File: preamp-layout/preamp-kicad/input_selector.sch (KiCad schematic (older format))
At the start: 40 parts, among them J54 Conn_01x03_Female, J55 Conn_01x03_Male, J56 Conn_01x03_Male, J57 Conn_01x03_Male, J58 Conn_01x03_Male, J59 Conn_01x07_Female, J60 Conn_01x07_Female, J61 Conn_01x03_Male, J62 Conn_01x03_Male, J63 Conn_01x03_Female, J64 Conn_01x02_Female, J65 Conn_01x02_Male, J66 Conn_01x03_Female, J67 Conn_01x03_Female, K1 G6JU, K2 G6JU, K3 G6JU, K4 G6JU, K5 G6JU, K6 G6JU, K7 G6JU, U17 MCP23S17_SP, U18 ULN2003, U19 ULN2003

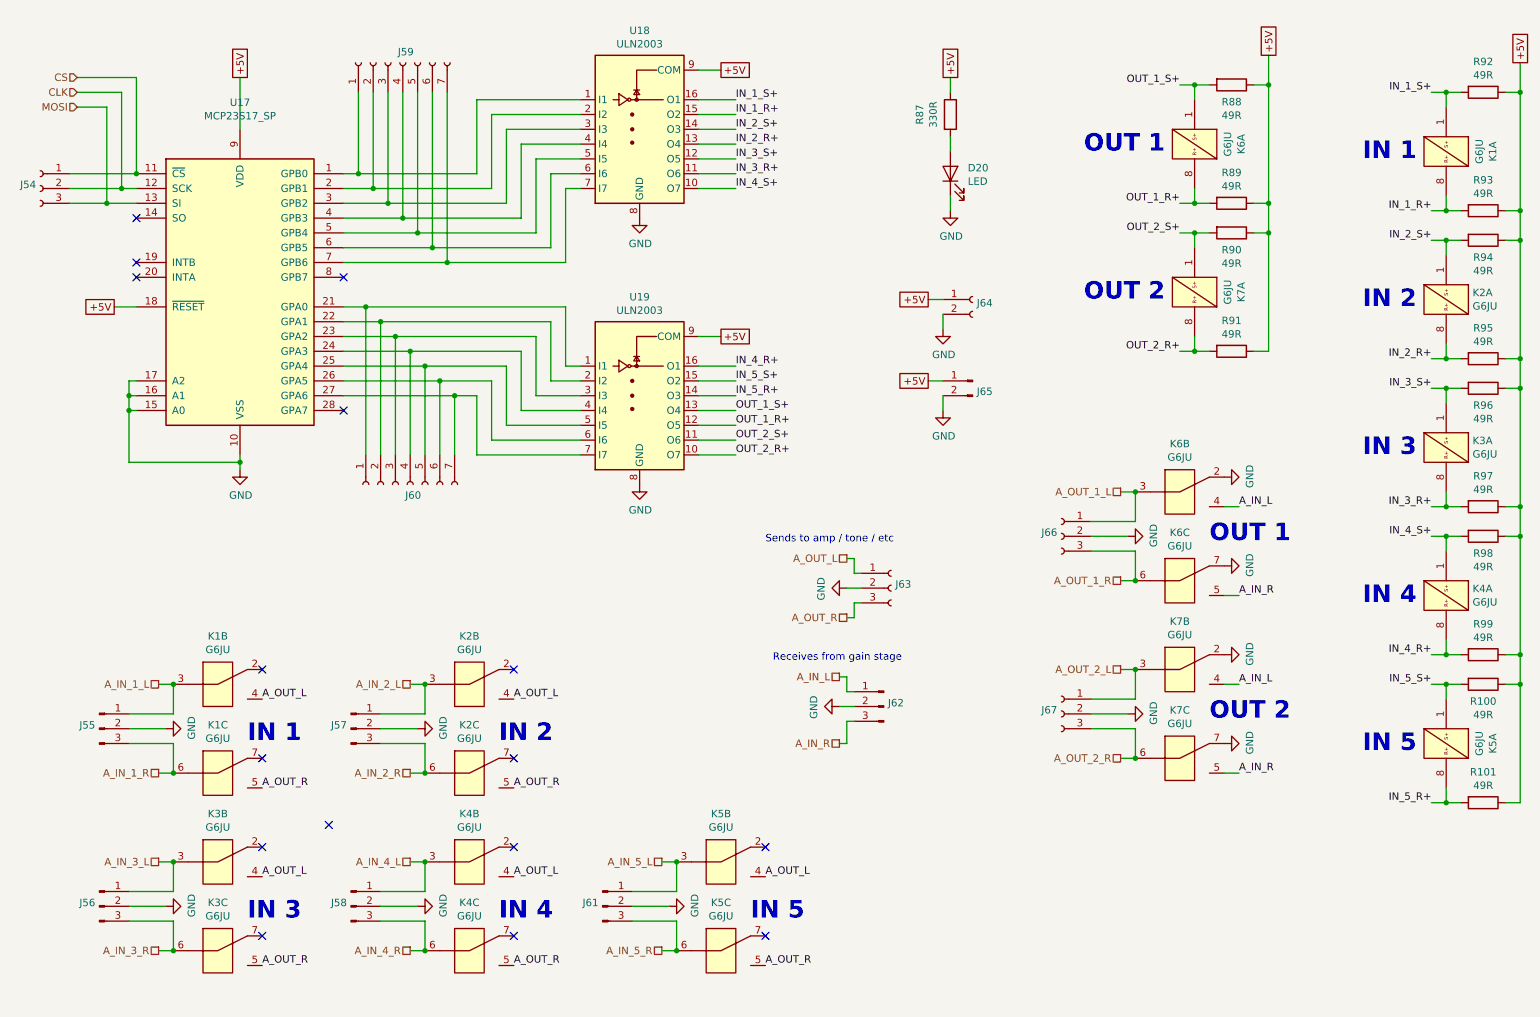
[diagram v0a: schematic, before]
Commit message: AC PCB Update
Removed Switch symbol from PCB, moved to main sheet. Started playing with footprint assignment. Other minor updates.
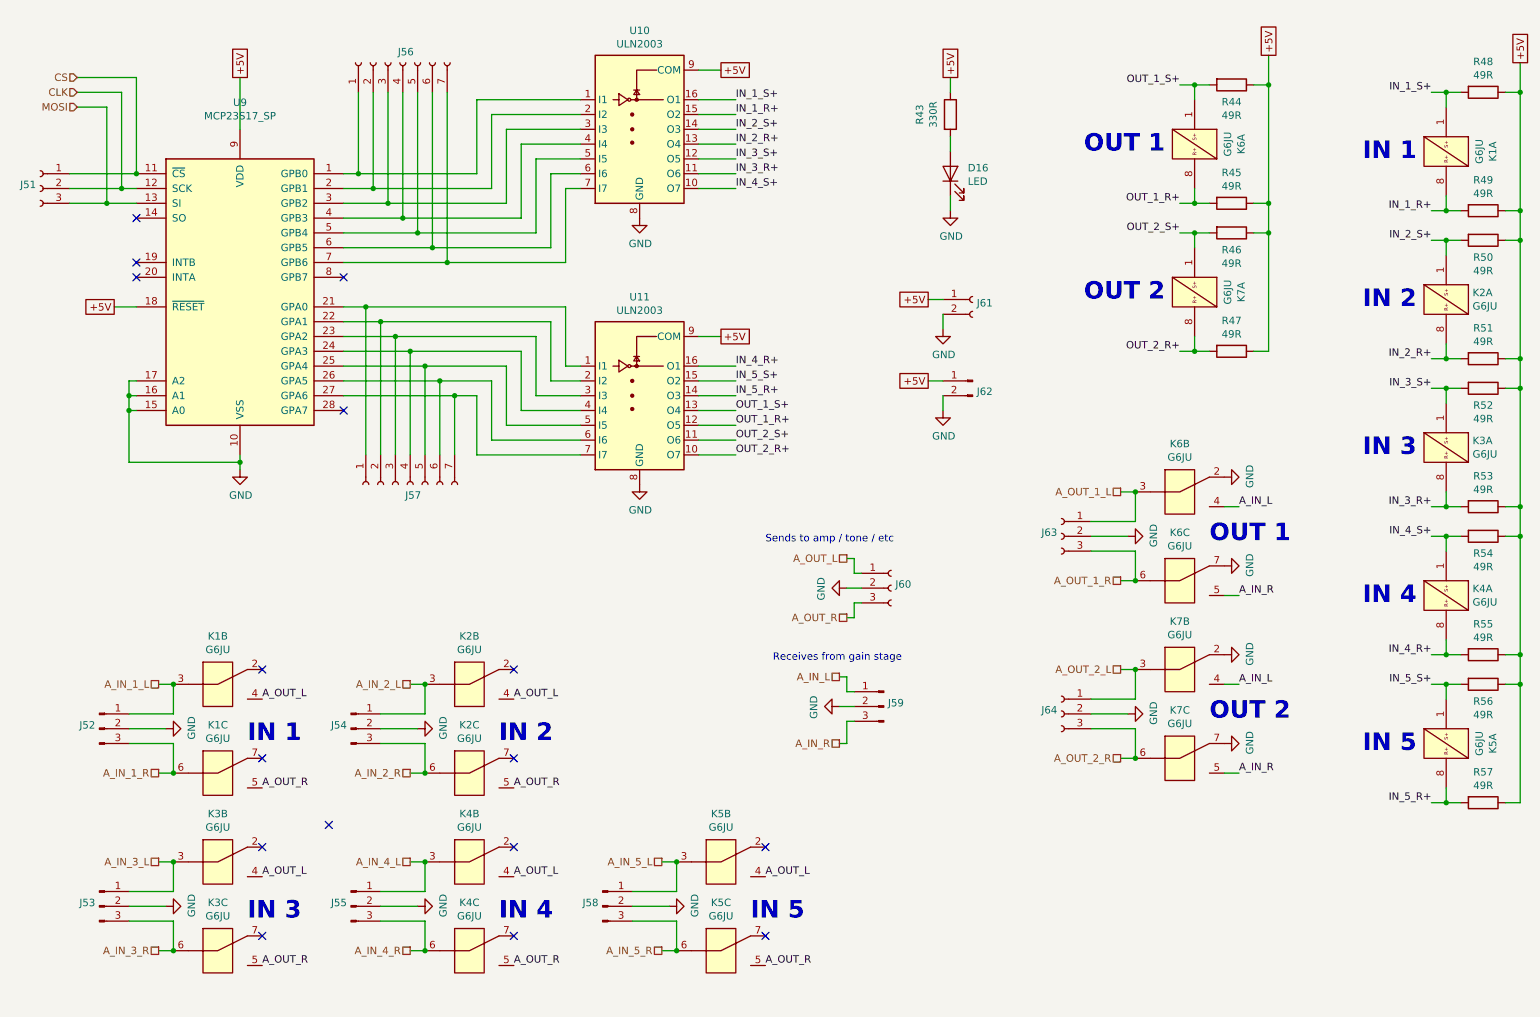
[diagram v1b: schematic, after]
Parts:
- renumbered D20 to D16, J54 to J51, J55 to J52, J56 to J53, J57 to J54, J58 to J55, J59 to J56, J60 to J57, J61 to J58, J62 to J59, J63 to J60, J64 to J61, J65 to J62, J66 to J63, J67 to J64, R87 to R43, R88 to R44, R89 to R45, R90 to R46, R91 to R47, R92 to R48, R93 to R49, R94 to R50, R95 to R51, R96 to R52, R97 to R53, R98 to R54, R99 to R55, R100 to R56, R101 to R57, U18 to U10, U19 to U11, U17 to U9

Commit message: Initial Footprint Assignment
Assigned footprints to SMT resistors, pin headers, screw terminals, LEDs, DIP-8 ICs
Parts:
- D16: footprint (none) -> LED_SMD:LED_1206_3216Metric_Pad1.42x1.75mm_HandSolder
- J51, J52, J53, J54, J55, J58, J59, J60, J63, J64: footprint (none) -> Connector_PinHeader_2.54mm:PinHeader_1x03_P2.54mm_Vertical
- J61, J62: footprint (none) -> Connector_PinHeader_2.54mm:PinHeader_1x02_P2.54mm_Vertical
- R43, R44, R45, R46, R47, R48, R49, R50, R51, R52, R53, R54, R55, R56, R57: footprint (none) -> Resistor_SMD:R_1206_3216Metric_Pad1.42x1.75mm_HandSolder
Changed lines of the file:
@@
 F 0 "J60" H 6628 4726 50  0000 L CNN
 F 1 "Conn_01x03_Female" H 6628 4635 50  0001 L CNN
-F 2 "" H 6600 4700 50  0001 C CNN
+F 2 "Connector_PinHeader_2.54mm:PinHeader_1x03_P2.54mm_Vertical" H 6600 4700 50  0001 C CNN
 F 3 "~" H 6600 4700 50  0001 C CNN
 	1    6600 4700
@@
 F 0 "R43" V 6793 1500 50  0000 C CNN
 F 1 "330R" V 6884 1500 50  0000 C CNN
-F 2 "" V 6930 1500 50  0001 C CNN
+F 2 "Resistor_SMD:R_1206_3216Metric_Pad1.42x1.75mm_HandSolder" V 6930 1500 50  0001 C CNN
 F 3 "~" H 7000 1500 50  0001 C CNN
 	1    7000 1500
@@
 F 0 "D16" V 7039 1783 50  0000 R CNN
 F 1 "LED" V 6948 1783 50  0000 R CNN
-F 2 "" H 7000 1900 50  0001 C CNN
+F 2 "LED_SMD:LED_1206_3216Metric_Pad1.42x1.75mm_HandSolder" H 7000 1900 50  0001 C CNN
 F 3 "~" H 7000 1900 50  0001 C CNN
 	1    7000 1900
@@
 F 0 "J59" H 6522 5524 50  0000 R CNN
 F 1 "Conn_01x03_Male" H 6522 5433 50  0001 R CNN
-F 2 "" H 6550 5500 50  0001 C CNN
+F 2 "Connector_PinHeader_2.54mm:PinHeader_1x03_P2.54mm_Vertical" H 6550 5500 50  0001 C CNN
 F 3 "~" H 6550 5500 50  0001 C CNN
 	1    6550 5500
@@
 F 0 "J61" H 7178 2726 50  0000 L CNN
 F 1 "Conn_01x02_Female" H 7178 2635 50  0001 L CNN
-F 2 "" H 7150 2750 50  0001 C CNN
+F 2 "Connector_PinHeader_2.54mm:PinHeader_1x02_P2.54mm_Vertical" H 7150 2750 50  0001 C CNN
 F 3 "~" H 7150 2750 50  0001 C CNN
 	1    7150 2750
@@
 F 0 "J62" H 7122 3228 50  0000 R CNN
 F 1 "Conn_01x02_Male" H 7122 3183 50  0001 R CNN
-F 2 "" H 7150 3300 50  0001 C CNN
+F 2 "Connector_PinHeader_2.54mm:PinHeader_1x02_P2.54mm_Vertical" H 7150 3300 50  0001 C CNN
 F 3 "~" H 7150 3300 50  0001 C CNN
 	1    7150 3300
@@
 F 0 "J51" H 878 2026 50  0000 L CNN
 F 1 "Conn_01x03_Female" H 878 1935 50  0001 L CNN
-F 2 "" H 850 2000 50  0001 C CNN
+F 2 "Connector_PinHeader_2.54mm:PinHeader_1x03_P2.54mm_Vertical" H 850 2000 50  0001 C CNN
 F 3 "~" H 850 2000 50  0001 C CNN
 	1    850  2000
@@
 F 0 "J52" H 1222 5674 50  0000 R CNN
 F 1 "Conn_01x03_Male" H 1222 5583 50  0001 R CNN
-F 2 "" H 1250 5650 50  0001 C CNN
+F 2 "Connector_PinHeader_2.54mm:PinHeader_1x03_P2.54mm_Vertical" H 1250 5650 50  0001 C CNN
 F 3 "~" H 1250 5650 50  0001 C CNN
 	1    1250 5650
@@
 F 0 "R48" V 10393 1350 50  0000 C CNN
 F 1 "49R" V 10484 1350 50  0000 C CNN
-F 2 "" V 10530 1350 50  0001 C CNN
+F 2 "Resistor_SMD:R_1206_3216Metric_Pad1.42x1.75mm_HandSolder" V 10530 1350 50  0001 C CNN
 F 3 "~" H 10600 1350 50  0001 C CNN
 	1    10600 1350
-	0    1    1    0
-$EndComp
-$Comp
-L Device:R R49
-U 1 1 632C72D5
-P 10600 2150
-AR Path="/5E2D8DA2/632C72D5" Ref="R49"  Part="1"
-AR Path="/632C72D5" Ref="R?"  Part="1"
-F 0 "R49" V 10393 2150 50  0000 C CNN
-F 1 "49R" V 10484 2150 50  0000 C CNN
-F 2 "" V 10530 2150 50  0001 C CNN
-F 3 "~" H 10600 2150 50  0001 C CNN
-	1    10600 2150
 	0    1    1    0
 $EndComp
@@
 F 0 "R50" V 10715 2350 50  0000 C CNN
 F 1 "49R" V 10806 2350 50  0000 C CNN
-F 2 "" V 10530 2350 50  0001 C CNN
+F 2 "Resistor_SMD:R_1206_3216Metric_Pad1.42x1.75mm_HandSolder" V 10530 2350 50  0001 C CNN
 F 3 "~" H 10600 2350 50  0001 C CNN
 	1    10600 2350
@@
 F 0 "R51" V 10393 3150 50  0000 C CNN
 F 1 "49R" V 10484 3150 50  0000 C CNN
-F 2 "" V 10530 3150 50  0001 C CNN
+F 2 "Resistor_SMD:R_1206_3216Metric_Pad1.42x1.75mm_HandSolder" V 10530 3150 50  0001 C CNN
 F 3 "~" H 10600 3150 50  0001 C CNN
 	1    10600 3150
@@
 F 0 "R52" V 10715 3350 50  0000 C CNN
 F 1 "49R" V 10806 3350 50  0000 C CNN
-F 2 "" V 10530 3350 50  0001 C CNN
+F 2 "Resistor_SMD:R_1206_3216Metric_Pad1.42x1.75mm_HandSolder" V 10530 3350 50  0001 C CNN
 F 3 "~" H 10600 3350 50  0001 C CNN
 	1    10600 3350
@@
 F 0 "R53" V 10393 4150 50  0000 C CNN
 F 1 "49R" V 10484 4150 50  0000 C CNN
-F 2 "" V 10530 4150 50  0001 C CNN
+F 2 "Resistor_SMD:R_1206_3216Metric_Pad1.42x1.75mm_HandSolder" V 10530 4150 50  0001 C CNN
 F 3 "~" H 10600 4150 50  0001 C CNN
 	1    10600 4150
@@
 F 0 "R54" V 10715 4350 50  0000 C CNN
 F 1 "49R" V 10806 4350 50  0000 C CNN
-F 2 "" V 10530 4350 50  0001 C CNN
+F 2 "Resistor_SMD:R_1206_3216Metric_Pad1.42x1.75mm_HandSolder" V 10530 4350 50  0001 C CNN
 F 3 "~" H 10600 4350 50  0001 C CNN
 	1    10600 4350
@@
 F 0 "R55" V 10393 5150 50  0000 C CNN
 F 1 "49R" V 10484 5150 50  0000 C CNN
-F 2 "" V 10530 5150 50  0001 C CNN
+F 2 "Resistor_SMD:R_1206_3216Metric_Pad1.42x1.75mm_HandSolder" V 10530 5150 50  0001 C CNN
 F 3 "~" H 10600 5150 50  0001 C CNN
 	1    10600 5150
@@
 F 0 "R56" V 10715 5350 50  0000 C CNN
 F 1 "49R" V 10806 5350 50  0000 C CNN
-F 2 "" V 10530 5350 50  0001 C CNN
+F 2 "Resistor_SMD:R_1206_3216Metric_Pad1.42x1.75mm_HandSolder" V 10530 5350 50  0001 C CNN
 F 3 "~" H 10600 5350 50  0001 C CNN
 	1    10600 5350
@@
 F 0 "R57" V 10393 6150 50  0000 C CNN
 F 1 "49R" V 10484 6150 50  0000 C CNN
-F 2 "" V 10530 6150 50  0001 C CNN
+F 2 "Resistor_SMD:R_1206_3216Metric_Pad1.42x1.75mm_HandSolder" V 10530 6150 50  0001 C CNN
 F 3 "~" H 10600 6150 50  0001 C CNN
 	1    10600 6150
@@
 F 0 "R44" V 9015 1300 50  0000 C CNN
 F 1 "49R" V 9106 1300 50  0000 C CNN
-F 2 "" V 8830 1300 50  0001 C CNN
+F 2 "Resistor_SMD:R_1206_3216Metric_Pad1.42x1.75mm_HandSolder" V 8830 1300 50  0001 C CNN
 F 3 "~" H 8900 1300 50  0001 C CNN
 	1    8900 1300
@@
 F 0 "R45" V 8693 2100 50  0000 C CNN
 F 1 "49R" V 8784 2100 50  0000 C CNN
-F 2 "" V 8830 2100 50  0001 C CNN
+F 2 "Resistor_SMD:R_1206_3216Metric_Pad1.42x1.75mm_HandSolder" V 8830 2100 50  0001 C CNN
 F 3 "~" H 8900 2100 50  0001 C CNN
 	1    8900 2100
@@
 F 0 "R46" V 9015 2300 50  0000 C CNN
 F 1 "49R" V 9106 2300 50  0000 C CNN
-F 2 "" V 8830 2300 50  0001 C CNN
+F 2 "Resistor_SMD:R_1206_3216Metric_Pad1.42x1.75mm_HandSolder" V 8830 2300 50  0001 C CNN
 F 3 "~" H 8900 2300 50  0001 C CNN
 	1    8900 2300
@@
 F 0 "R47" V 8693 3100 50  0000 C CNN
 F 1 "49R" V 8784 3100 50  0000 C CNN
-F 2 "" V 8830 3100 50  0001 C CNN
+F 2 "Resistor_SMD:R_1206_3216Metric_Pad1.42x1.75mm_HandSolder" V 8830 3100 50  0001 C CNN
 F 3 "~" H 8900 3100 50  0001 C CNN
 	1    8900 3100
@@
 F 0 "J64" H 7778 5576 50  0000 L CNN
 F 1 "Conn_01x03_Female" H 7778 5485 50  0001 L CNN
-F 2 "" H 7750 5550 50  0001 C CNN
+F 2 "Connector_PinHeader_2.54mm:PinHeader_1x03_P2.54mm_Vertical" H 7750 5550 50  0001 C CNN
 F 3 "~" H 7750 5550 50  0001 C CNN
 	1    7750 5550
@@
 F 0 "J63" H 7778 4376 50  0000 L CNN
 F 1 "Conn_01x03_Female" H 7778 4285 50  0001 L CNN
-F 2 "" H 7750 4350 50  0001 C CNN
+F 2 "Connector_PinHeader_2.54mm:PinHeader_1x03_P2.54mm_Vertical" H 7750 4350 50  0001 C CNN
 F 3 "~" H 7750 4350 50  0001 C CNN
 	1    7750 4350
@@
 F 0 "J54" H 2922 5674 50  0000 R CNN
 F 1 "Conn_01x03_Male" H 2922 5583 50  0001 R CNN
-F 2 "" H 2950 5650 50  0001 C CNN
+F 2 "Connector_PinHeader_2.54mm:PinHeader_1x03_P2.54mm_Vertical" H 2950 5650 50  0001 C CNN
 F 3 "~" H 2950 5650 50  0001 C CNN
 	1    2950 5650
@@
 F 0 "J53" H 1222 6874 50  0000 R CNN
 F 1 "Conn_01x03_Male" H 1222 6783 50  0001 R CNN
-F 2 "" H 1250 6850 50  0001 C CNN
+F 2 "Connector_PinHeader_2.54mm:PinHeader_1x03_P2.54mm_Vertical" H 1250 6850 50  0001 C CNN
 F 3 "~" H 1250 6850 50  0001 C CNN
 	1    1250 6850
@@
 F 0 "J55" H 2922 6874 50  0000 R CNN
 F 1 "Conn_01x03_Male" H 2922 6783 50  0001 R CNN
-F 2 "" H 2950 6850 50  0001 C CNN
+F 2 "Connector_PinHeader_2.54mm:PinHeader_1x03_P2.54mm_Vertical" H 2950 6850 50  0001 C CNN
 F 3 "~" H 2950 6850 50  0001 C CNN
 	1    2950 6850
@@
 F 0 "J58" H 4622 6874 50  0000 R CNN
 F 1 "Conn_01x03_Male" H 4622 6783 50  0001 R CNN
-F 2 "" H 4650 6850 50  0001 C CNN
+F 2 "Connector_PinHeader_2.54mm:PinHeader_1x03_P2.54mm_Vertical" H 4650 6850 50  0001 C CNN
 F 3 "~" H 4650 6850 50  0001 C CNN
 	1    4650 6850
@@
 $EndComp
 NoConn ~ 2800 6300
+$Comp
+L Device:R R49
+U 1 1 632C72D5
+P 10600 2150
+AR Path="/5E2D8DA2/632C72D5" Ref="R49"  Part="1"
+AR Path="/632C72D5" Ref="R?"  Part="1"
+F 0 "R49" V 10393 2150 50  0000 C CNN
+F 1 "49R" V 10484 2150 50  0000 C CNN
+F 2 "Resistor_SMD:R_1206_3216Metric_Pad1.42x1.75mm_HandSolder" V 10530 2150 50  0001 C CNN
+F 3 "~" H 10600 2150 50  0001 C CNN
+	1    10600 2150
+	0    1    1    0
+$EndComp
 $EndSCHEMATC

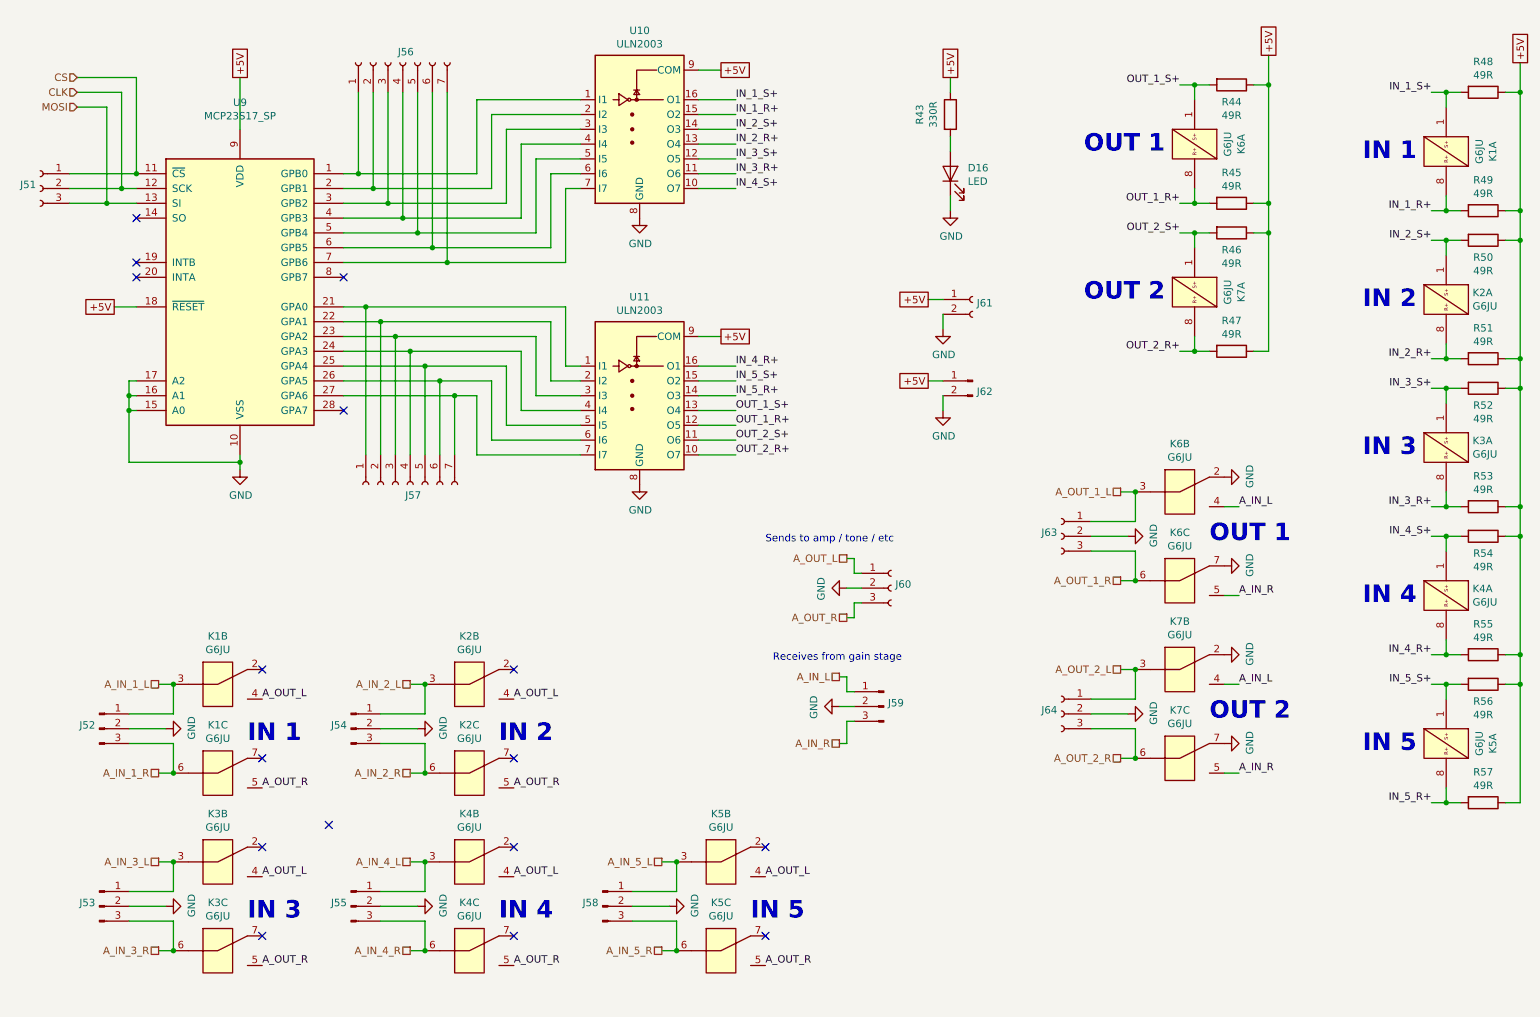
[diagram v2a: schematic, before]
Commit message: BOM update
Minor changes to schematic, value changes and footprint entry. BOM updated with parts sourcing
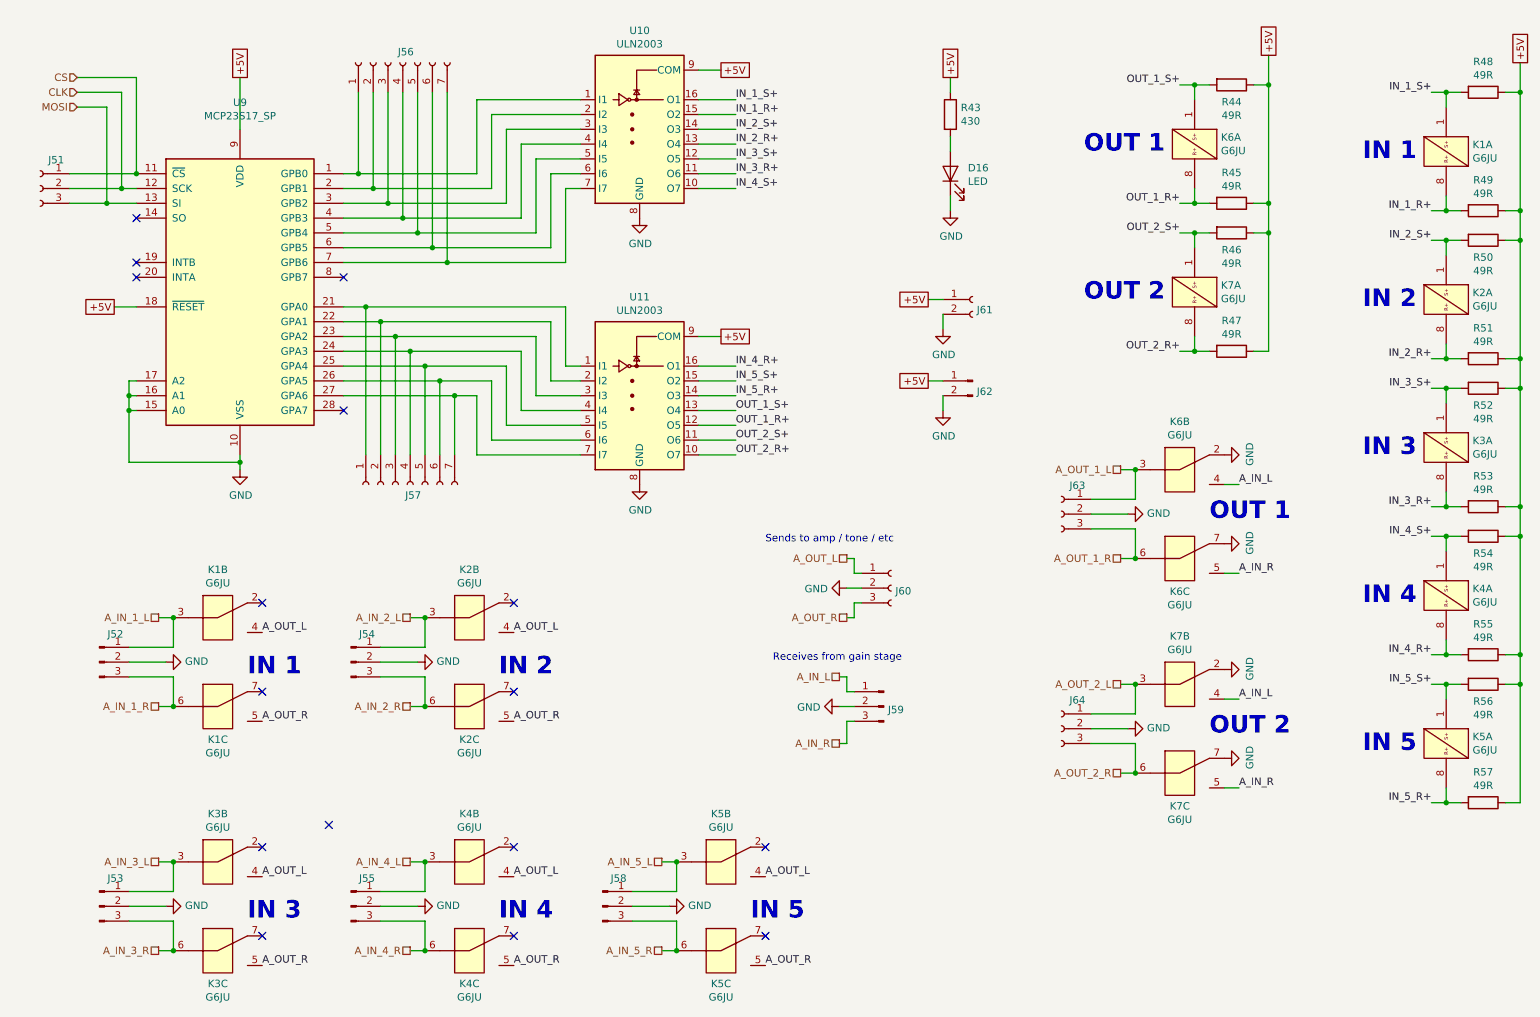
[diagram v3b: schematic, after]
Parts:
- R43: value 330R -> 430
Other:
- moved on the sheet: J52, J54, J63, J64, K1B, K1C, K2B, K2C, K6B, K6C, K7B, K7C
